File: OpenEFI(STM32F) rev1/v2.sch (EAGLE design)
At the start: 133 parts, among them IC1 4050N, IC10 LM358D, IC11 74HC595D, IC12 74HC595D, IC2 LM358D, IC3 4067D, IC5 4050N, IC6 74HC164D, IC7 4051D, IC8 24AA08SN, IC9 LM358D, P1 39-30-06, Q1 MJD122, Q10 MJD122, Q11 MJD122, Q13 MJD122, Q15 MJD122, Q16 MJD122, Q17 MJD122, Q2 BC548, Q3 MJD122, Q5 MJD122, Q7 MJD122, Q9 MJD122, U1 ATMEGA328P-AU

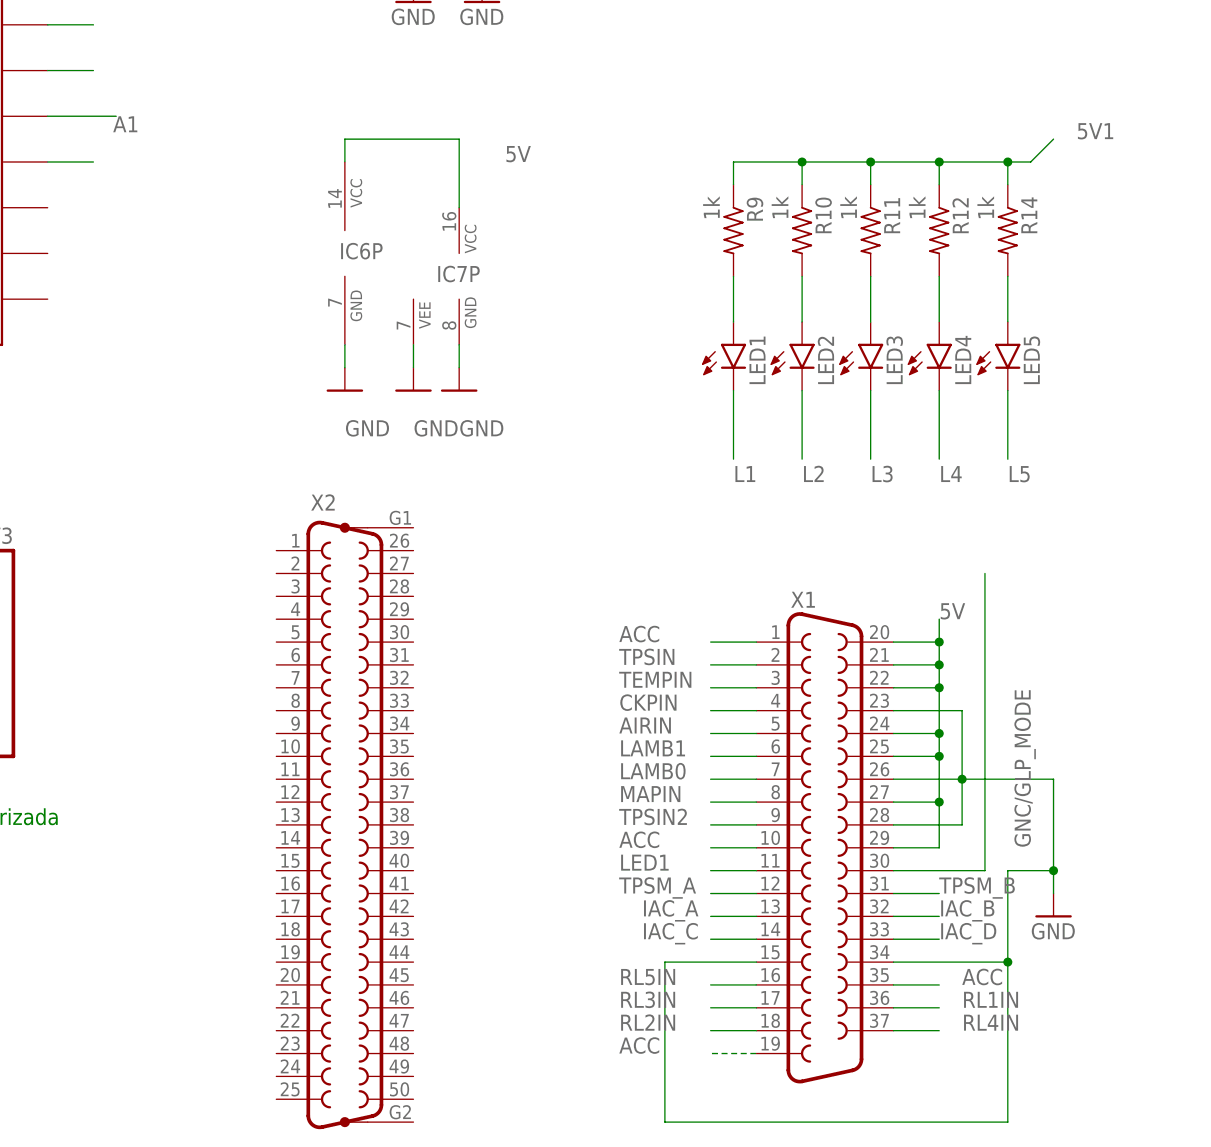
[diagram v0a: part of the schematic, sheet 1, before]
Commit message: Creacion de V2 del PCB para SMT32F
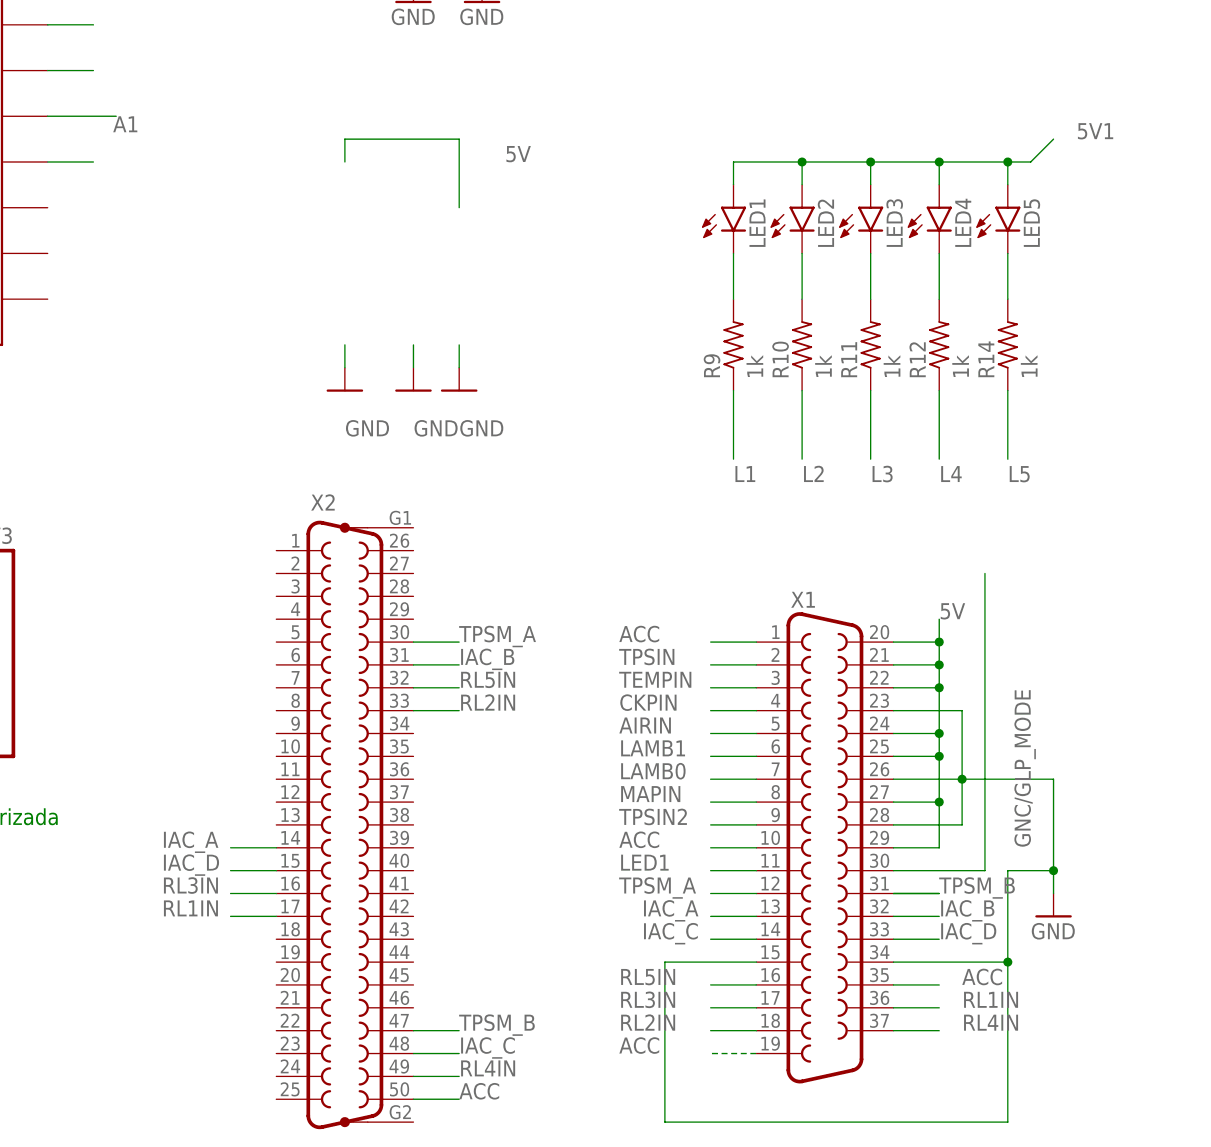
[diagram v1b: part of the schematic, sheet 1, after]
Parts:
- removed IC1: 4050N, 40xx:4050N
- removed IC6: 74HC164D, 74xx-us:74HC164D
- removed IC7: 4051D, 40xx:4051D
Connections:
- net 5V: now also IC3P.VDD; no longer IC6P.VCC, IC7P.VCC
- net 5V1: now also LED1.A, LED2.A, LED3.A, LED4.A, LED5.A; no longer R10.1, R11.1, R12.1, R14.1, R9.1
- net ACC: now also IC5P.VDD, X2.50; no longer IC1P.VDD
- net GND: now also IC3P.VSS, IC5P.VSS; no longer IC1P.VSS, IC6P.GND, IC7P.GND, IC7P.VEE
- net IAC_A: now also X2.14
- net IAC_B: now also X2.31
- net IAC_C: now also X2.48
- net IAC_D: now also X2.15
- net L1: now also R9.1; no longer LED1.C
- net L2: now also R10.1; no longer LED2.C
- net L3: now also R11.1; no longer LED3.C
- net L4: now also R12.1; no longer LED4.C
- net L5: now also R14.1; no longer LED5.C
- net N$12: now also LED1.C; no longer LED1.A
- net N$13: now also LED2.C; no longer LED2.A
- net N$15: now also LED3.C; no longer LED3.A
- net N$16: now also LED4.C; no longer LED4.A
- net N$17: now also LED5.C; no longer LED5.A
- net RL1IN: now also X2.17
- net RL2IN: now also X2.33
- net RL3IN: now also X2.16
- net RL4IN: now also X2.49
- net RL5IN: now also X2.32
- net TPSM_A: now also X2.30
- net TPSM_B: now also X2.47
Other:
- moved on the sheet: LED1, LED2, LED3, LED4, LED5, R10, R11, R12, R14, R9

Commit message: cambios menores
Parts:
- removed IC10: LM358D, linear:LM358D
- removed X1: (no value), con-subd:F37HP
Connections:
- removed net AIRIN: X1.5
- removed net AUX6: IC3A.X15
- removed net MAPIN: X1.8
- removed net TEMPIN: X1.3
- removed net TPSIN: X1.2
- removed net TPSIN2: X1.9
- net 5V: no longer IC10P.V+, X1.20, X1.21, X1.22, X1.24, X1.25, X1.27, X1.29
- net ACC: no longer X1.1, X1.10, X1.19, X1.35
- net AOUT0: now also IC3A.X7; no longer IC3A.X0
- net AOUT1: now also IC3A.X6; no longer IC3A.X1
- net AOUT2: now also IC3A.X5; no longer IC3A.X2
- net AOUT3: now also IC3A.X4; no longer IC3A.X3
- net AOUT4: now also IC3A.X3; no longer IC3A.X4
- net AOUT5: now also IC3A.X2; no longer IC3A.X5
- net AOUT6: now also IC3A.X1; no longer IC3A.X6
- net AOUT7: now also IC3A.X0; no longer IC3A.X7
- net AUX1: now also IC3A.X11; no longer IC3A.X10
- net AUX2: now also IC3A.X12; no longer IC3A.X11
- net AUX3: now also IC3A.X13; no longer IC3A.X12
- net AUX4: now also IC3A.X14; no longer IC3A.X13
- net AUX5: now also IC3A.X15; no longer IC3A.X14
- net CKPIN: no longer X1.4
- net GNC/GLP_MODE: no longer X1.30
- net GND: no longer IC10P.V-, X1.15, X1.23, X1.26, X1.28, X1.34
- net IAC_A: no longer X1.13
- net IAC_B: no longer X1.32
- net IAC_C: no longer X1.14
- net IAC_D: no longer X1.33
- net LAMB0: no longer X1.7
- net LAMB1: no longer X1.6
- net LAMB1OUT: now also IC9B.OUT; no longer IC10A.OUT
- net LED1: no longer X1.11
- net N$1: now also IC9B.+IN; no longer IC10A.+IN
- net N$37: now also IC9B.-IN; no longer IC10A.-IN
- net RL1IN: no longer X1.36
- net RL2IN: no longer X1.18
- net RL3IN: no longer X1.17
- net RL4IN: no longer X1.37
- net RL5IN: no longer X1.16
- net TPSM_A: no longer X1.12
- net TPSM_B: no longer X1.31
- net VBAT: now also IC3A.X10
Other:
- note added: "321194"

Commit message: Avances en I/O en rev1
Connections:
- net N$18 renamed N$18_P
- net N$20 renamed N$20_N
- net AIN0: now also X2.13
- net AIN1: now also X2.29
- net AIN4: now also X2.12
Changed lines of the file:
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@@
+</segment>
+</net>
+<net name="AIN0" class="0">
+<segment>
+<pinref part="X2" gate="G$1" pin="13"/>
+<wire x1="2.54" y1="-157.48" x2="-2.54" y2="-157.48" width="0.1524" layer="91"/>
+<label x="-10.16" y="-157.48" size="1.778" layer="95"/>
+</segment>
+</net>
+<net name="AIN1" class="0">
+<segment>
+<pinref part="X2" gate="G$1" pin="29"/>
+<wire x1="17.78" y1="-134.62" x2="22.86" y2="-134.62" width="0.1524" layer="91"/>
+<label x="22.86" y="-134.62" size="1.778" layer="95"/>
+</segment>
+</net>
+<net name="AIN4" class="0">
+<segment>
+<pinref part="X2" gate="G$1" pin="12"/>
+<wire x1="2.54" y1="-154.94" x2="-2.54" y2="-154.94" width="0.1524" layer="91"/>
+<label x="-10.16" y="-154.94" size="1.778" layer="95"/>
 </segment>
 </net>
@@
 </segment>
 </net>
-<net name="N$18" class="0">
+<net name="N$18_P" class="0">
 <segment>
 <pinref part="Q4" gate="G$1" pin="2"/>
@@
 <wire x1="-12.7" y1="27.94" x2="12.7" y2="27.94" width="0.1524" layer="91"/>
 <pinref part="U1" gate="A" pin="PB6"/>
-</segment>
-</net>
-<net name="N$20" class="0">
+<label x="-17.78" y="25.4" size="1.778" layer="95"/>
+</segment>
+</net>
+<net name="N$20_N" class="0">
 <segment>
 <pinref part="Q4" gate="G$1" pin="1"/>
@@
 <pinref part="U1" gate="A" pin="PB7"/>
 <wire x1="0" y1="25.4" x2="12.7" y2="25.4" width="0.1524" layer="91"/>
-</segment>
-</net>
+<label x="2.54" y="22.86" size="1.778" layer="95"/>
+</segment>
+</net>

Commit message: init v3
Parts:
- removed 1K-1%, 3K-1%: 520, rcl:R-EU_0204/7
- removed C10, C3: (no value), rcl:CPOL-EUE3.5-8
- removed D21, D22, D23, D32, D33: S1M, diode:S1M
- removed IC4: (no value), linear:LM2596S
- removed IC5: 4050N, 40xx:4050N
- removed L1: 68uH, inductor-neosid:SD12-680
- removed Q17: MJD122, MJD122:MJD122
- removed U1: ATMEGA328P-AU, atmega328:ATMEGA328P-AU
- added D11: 1N4148DO35-7, diode:1N4148DO35-7
- added D25: BZY97, diode:BZY97
- added F2: (no value), fuse:TE5
- added J1, J2: 1053141206, 1053141206:1053141206
- added P3: 39-30-04, con-molex-mini-fit:39-30-04
- added Q12, Q19, Q22, Q25: BC558A, transistor-pnp:BC558A
- added Q14, Q20, Q23, Q6: IRLZ44Z, transistor-power:IRLZ44Z
- added Q18, Q21, Q24, Q8: BC548, transistor-npn:BC548
- added Q26: BD139, transistor-power:BD139
- added R15, R51: 1k, rcl:R-US_0204/5
- added R31, R32, R33, R34, R43, R44, R45, R46, R47, R48, R49, R50: (no value), rcl:R-EU_0207/10
- added X1, X3: (no value), con-subd:F15HP
- D1, D16, D4, D6, D7: value 1N4004 -> BZY97; device diode:1N4004 -> diode:BZY97
- D12, D13, D14, D15, D20: value S1M -> 1N4446; device diode:S1M -> diode:1N4446
- D18: value 1N4004 -> 1N4148DO35-7; device diode:1N4004 -> diode:1N4148DO35-7
- D9: value Ss54 -> 1N4446; device s1x_10:S1A -> diode:1N4446
- Q1, Q7: value MJD122 -> IRLZ44Z; device MJD122:MJD122 -> transistor-power:IRLZ44Z
- Q10, Q15, Q16, Q9: value MJD122 -> BD139; device MJD122:MJD122 -> transistor-power:BD139
- Q11, Q3: value MJD122 -> BC548; device MJD122:MJD122 -> transistor-npn:BC548
- Q13, Q5: value MJD122 -> BC558A; device MJD122:MJD122 -> transistor-pnp:BC558A
- Q4: value (none) -> BD139; device special:XTAL/S -> transistor-power:BD139
- X2: value (none) -> MINI-USB_4P-85-32004-10X; device con-subd:F50HP -> con-cypressindustries:MINI-USB_4P-85-32004-10X
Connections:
- removed net ECN1: D16.C, P1.5, Q11.C
- removed net ECN1L: IC5E.I, U1.PC4
- removed net ECN2: D18.C, P1.6, Q13.C
- removed net ECN2L: IC5F.I, U1.PC5
- removed net N$18_P: Q4.2, U1.PB6
- removed net N$20_N: Q4.1, U1.PB7
- removed net N$91: D9.C, IC4.OUT, L1.1
- removed net N$92: 1K-1%.1, 3K-1%.2, IC4.FB
- new net 5V-USB: D11.A, X2.1
- new net D+: U$2.PA_12, X2.3
- new net D-: U$2.PA_11, X2.2
- new net GND2: F2.2, Q1.S, Q14.S, Q20.S, Q23.S, Q6.S, Q7.S
- new net INY5: D7.C, P1.5, Q20.D
- new net INY6: D16.C, P1.6, Q23.D
- new net INYL5A: R47.2
- new net INYL6A: R49.2
- new net N$18: Q13.B, Q8.B, R43.1
- new net N$20: Q13.E, Q8.E, R44.2
- new net N$27: Q7.G, R44.1
- new net N$28: Q18.B, Q19.B, R45.1
- new net N$30: Q18.E, Q19.E, R46.2
- new net N$33: Q14.G, R46.1
- new net N$35: D18.A, PROG.4
- new net N$36: Q4.B, R51.2
- new net N$46: Q21.B, Q22.B, R47.1
- new net N$47: Q21.E, Q22.E, R48.2
- new net N$48: Q20.G, R48.1
- new net N$49: Q24.B, Q25.B, R49.1
- new net N$50: Q24.E, Q25.E, R50.2
- new net N$52: Q23.G, R50.1
- new net RL6: R51.1
- new net RL6IN: D20.C, J1.6, Q4.C
- net 5V: no longer 3K-1%.1, C10.+, L1.2, U1.AREF, U1.AVCC, U1.VCC, U1.VCC_2
- net 5V1: now also D11.C, D18.C; no longer PROG.4
- net ACC: now also Q11.C, Q18.C, Q21.C, Q24.C, Q3.C, Q8.C; no longer C3.+, D13.C, D15.C, D21.C, D23.C, D33.C, IC4.IN, IC5P.VDD, X2.50
- net AIN0: no longer X2.13
- net AIN1: no longer X2.29
- net AIN4: no longer X2.12
- net CKPOUT: no longer U1.PD2
- net GND: now also D15.A, D25.A, F2.1, P3.1, P3.2, P3.3, P3.4, Q12.C, Q13.C, Q19.C, Q22.C, Q25.C, Q26.E, Q4.E, Q5.C, X2.4; no longer 1K-1%.2, C10.-, C3.-, D18.A, D22.A, D32.A, IC4.EN, IC4.GND, IC4.GND@1, IC5P.VSS, Q1.E, Q11.E, Q13.E, Q17.E, Q3.E, Q5.E, Q7.E, U1.GND, U1.GND_2, U1.GND_3
- net IAC_A: no longer X2.14
- net IAC_B: no longer X2.31
- net IAC_C: no longer X2.48
- net IAC_D: no longer X2.15
- net INY1: now also D25.C, Q6.D; no longer D1.C, Q1.C
- net INY2: now also D1.C, Q1.D; no longer D4.C, Q3.C
- net INY3: now also D4.C, Q7.D; no longer D6.C, Q5.C
- net INY4: now also D6.C, Q14.D; no longer D7.C, Q7.C
- net INYL1A: now also R31.2; no longer IC5A.I, U1.PC0
- net INYL2A: now also R33.2; no longer IC5B.I, U1.PC1
- net INYL3A: now also R43.2; no longer IC5C.I, U1.PC2
- net INYL4A: now also R45.2; no longer IC5D.I, U1.PC3
- net MISO: no longer U1.PB4
- net MOSI: no longer U1.PB3
- net N$10: now also Q1.G, R34.1; no longer IC5F.O, Q13.B
- net N$19: now also Q10.B; no longer Q15.B
- net N$2: now also Q11.B, Q12.B, R31.1; no longer IC5A.O, Q1.B
- net N$29: now also Q15.B; no longer Q16.B
- net N$3: now also Q11.E, Q12.E, R32.2; no longer IC5B.O, Q3.B
- net N$4: now also Q26.B; no longer Q9.B
- net N$5: now also Q3.B, R33.1; no longer IC5C.O
- net N$6: now also Q6.G, R32.1; no longer IC5D.O, Q7.B
- net N$7: now also Q16.B; no longer Q17.B
- net N$8: now also Q9.B; no longer Q10.B
- net N$9: now also Q3.E, Q5.E, R34.2; no longer IC5E.O, Q11.B
- net PWM: no longer U1.PD3
- net RCK: no longer U1.PD7
- net RL1IN: now also D9.C, J1.1, Q26.C; no longer D12.C, D13.A, Q9.C, X2.17
- net RL2IN: now also D12.C, J1.2, Q9.C; no longer D14.C, D15.A, Q10.C, X2.33
- net RL3IN: now also D13.C, J1.3, Q10.C; no longer D20.C, D21.A, Q15.C, X2.16
- net RL4IN: now also D14.C, J1.4, Q15.C; no longer D22.C, D23.A, Q16.C, X2.49
- net RL5IN: now also D15.C, J1.5, Q16.C; no longer D32.C, D33.A, Q17.C, X2.32
- net SCK: no longer U1.PB5
- net SCK2: no longer U1.PD6
- net SER: no longer U1.PD5
- net SS: no longer U1.PB2
- net TPSM_A: no longer X2.30
- net TPSM_B: no longer X2.47
